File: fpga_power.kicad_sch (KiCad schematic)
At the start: 1 part, among them U2 XC7A50T-2FTG256I

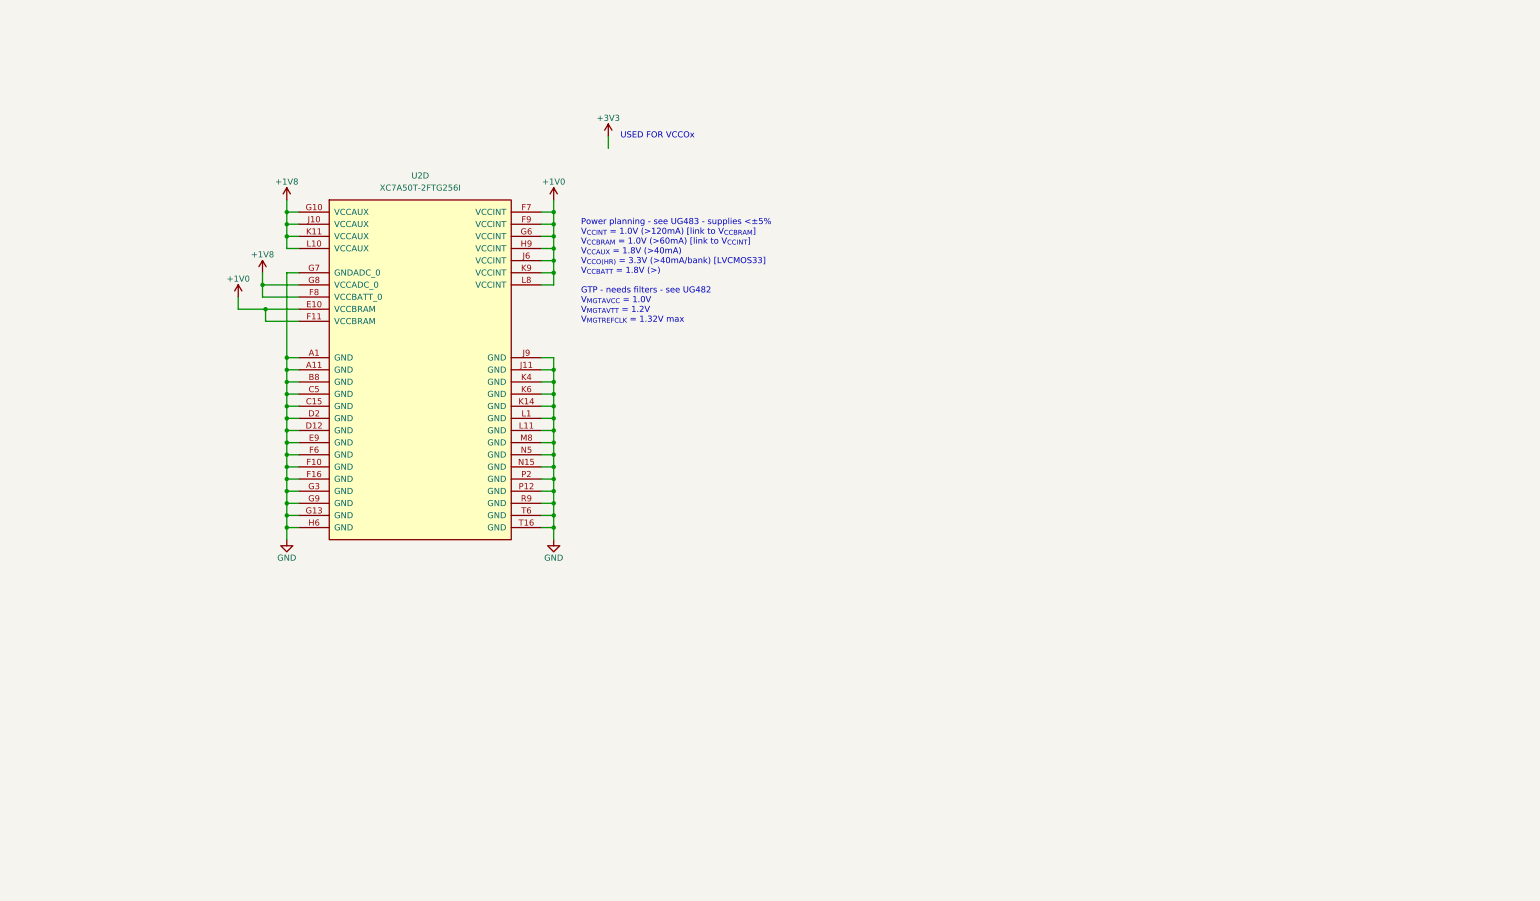
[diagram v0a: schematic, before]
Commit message: Changed FPGA to new package and hooked up some more pins
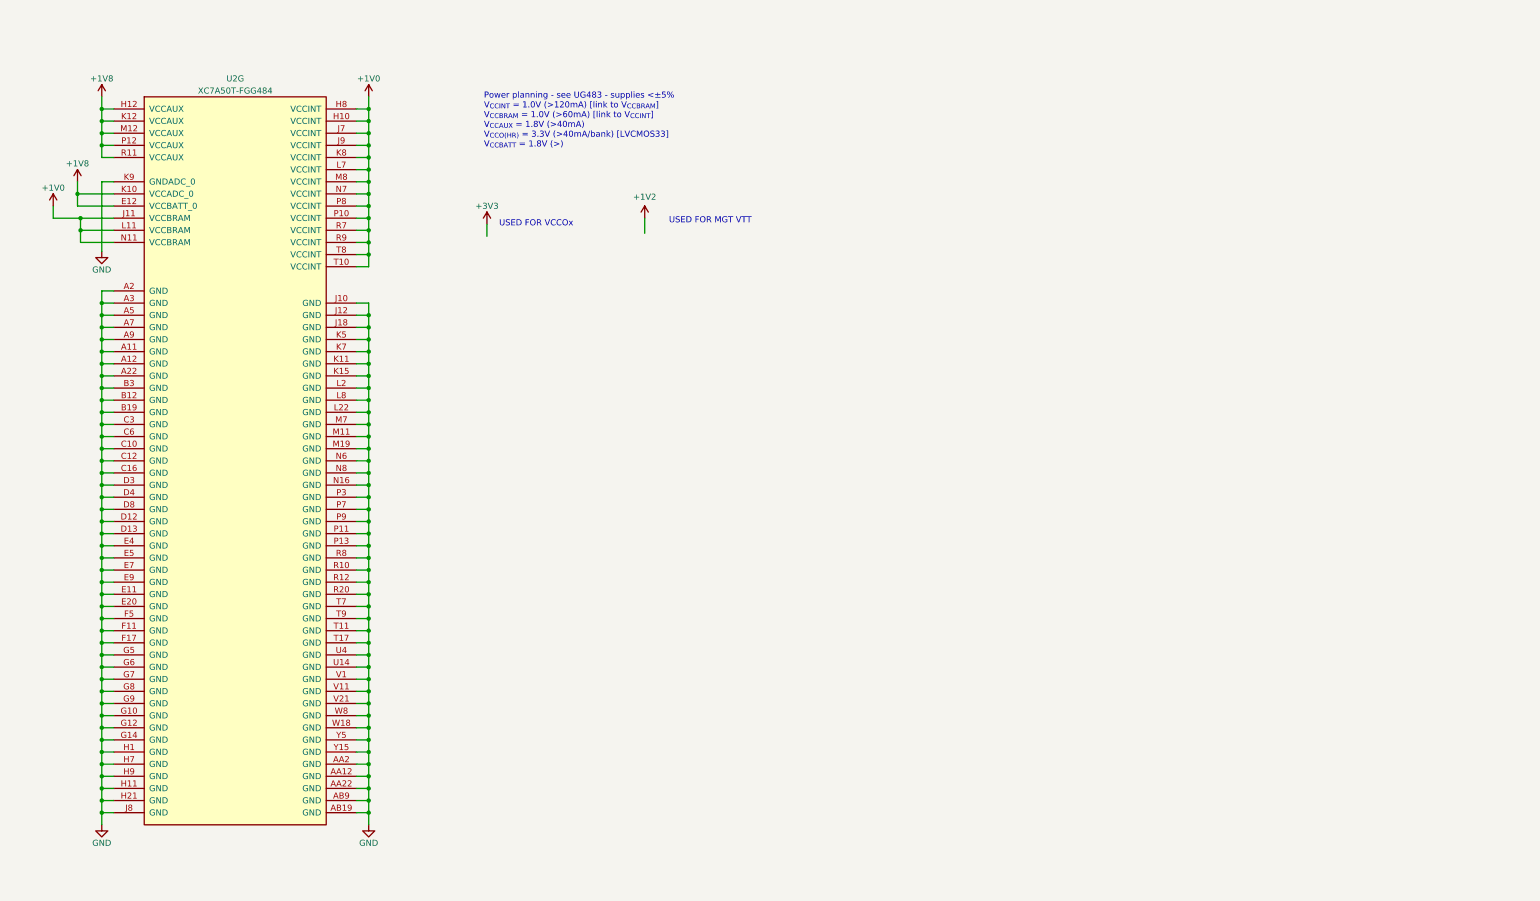
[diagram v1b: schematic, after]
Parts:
- removed U2: XC7A50T-2FTG256I, Package_BGA:Xilinx_FTG256, symbol FPGA_Xilinx_Artix7:XC7A50T-FTG256
- added U2: XC7A50T-FGG484, Package_BGA:Xilinx_FGG484, symbol FPGA_Xilinx_Artix7:XC7A50T-FGG484
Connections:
- net +1V0: now also U2.H10 (VCCINT), U2.H8 (VCCINT), U2.J11 (VCCBRAM), U2.J7 (VCCINT), U2.J9 (VCCINT), U2.K8 (VCCINT), U2.L11 (VCCBRAM), U2.L7 (VCCINT), U2.M8 (VCCINT), U2.N11 (VCCBRAM), U2.N7 (VCCINT), U2.P10 (VCCINT), U2.P8 (VCCINT), U2.R7 (VCCINT), U2.R9 (VCCINT), U2.T10 (VCCINT), U2.T8 (VCCINT)
- net +1V8: now also U2.E12 (VCCBATT_0), U2.H12 (VCCAUX), U2.K10 (VCCADC_0), U2.K12 (VCCAUX), U2.M12 (VCCAUX), U2.P12 (VCCAUX), U2.R11 (VCCAUX)
- net GND: now also U2.A11 (GND), U2.A12 (GND), U2.A2 (GND), U2.A22 (GND), U2.A3 (GND), U2.A5 (GND), U2.A7 (GND), U2.A9 (GND), U2.AA12 (GND), U2.AA2 (GND), U2.AA22 (GND), U2.AB19 (GND), U2.AB9 (GND), U2.B12 (GND), U2.B19 (GND), U2.B3 (GND), U2.C10 (GND), U2.C12 (GND), U2.C16 (GND), U2.C3 (GND), U2.C6 (GND), U2.D12 (GND), U2.D13 (GND), U2.D3 (GND), U2.D4 (GND), U2.D8 (GND), U2.E11 (GND), U2.E20 (GND), U2.E4 (GND), U2.E5 (GND), U2.E7 (GND), U2.E9 (GND), U2.F11 (GND), U2.F17 (GND), U2.F5 (GND), U2.G10 (GND), U2.G12 (GND), U2.G14 (GND), U2.G5 (GND), U2.G6 (GND), U2.G7 (GND), U2.G8 (GND), U2.G9 (GND), U2.H1 (GND), U2.H11 (GND), U2.H21 (GND), U2.H7 (GND), U2.H9 (GND), U2.J10 (GND), U2.J12 (GND), U2.J18 (GND), U2.J8 (GND), U2.K11 (GND), U2.K15 (GND), U2.K5 (GND), U2.K7 (GND), U2.K9 (GNDADC_0), U2.L2 (GND), U2.L22 (GND), U2.L8 (GND), U2.M11 (GND), U2.M19 (GND), U2.M7 (GND), U2.N16 (GND), U2.N6 (GND), U2.N8 (GND), U2.P11 (GND), U2.P13 (GND), U2.P3 (GND), U2.P7 (GND), U2.P9 (GND), U2.R10 (GND), U2.R12 (GND), U2.R20 (GND), U2.R8 (GND), U2.T11 (GND), U2.T17 (GND), U2.T7 (GND), U2.T9 (GND), U2.U14 (GND), U2.U4 (GND), U2.V1 (GND), U2.V11 (GND), U2.V21 (GND), U2.W18 (GND), U2.W8 (GND), U2.Y15 (GND), U2.Y5 (GND)
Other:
- note added: "Power planning - see UG483 - supplies <±5% V_{CCINT} = 1.0V (>120mA) [link to V_{CCBRAM}] V_{CCBRAM} = 1.0V (>60mA) [link to V_{CCINT}] V_{CCAUX} = 1.8V (>40mA) V_{CCO(HR)} = 3.3V (>40mA/bank) [LVCMOS33] V_{CCBATT} = 1.8V (>)"
- note added: "USED FOR MGT VTT"
- note removed: "Power planning - see UG483 - supplies <±5% V_{CCINT} = 1.0V (>120mA) [link to V_{CCBRAM}] V_{CCBRAM} = 1.0V (>60mA) [link to V_{CCINT}] V_{CCAUX} = 1.8V (>40mA) V_{CCO(HR)} = 3.3V (>40mA/bank) [LVCMOS33] V_{CCBATT} = 1.8V (>) GTP - needs filters - see UG482 V_{MGTAVCC} = 1.0V V_{MGTAVTT} = 1.2V V_{MGTREFCLK} = 1.32V max"

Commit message: Schematic finished, starting layout
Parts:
- added C100, C95, C96, C97, C98, C99: 100u, Capacitor_SMD:C_1206_3216Metric_Pad1.33x1.80mm_HandSolder, symbol Device:C_Small
- added C14, C16, C17, C20, C21, C22, C23, C25, C27, C28, C29, C30, C32, C34, C35, C36, C37, C39, C41, C42, C43, C44, C46, C48, C8, C9: 4.7u, Capacitor_SMD:C_0402_1005Metric_Pad0.74x0.62mm_HandSolder, symbol Device:C_Small
- added C18, C24: 4.7n, Capacitor_SMD:C_0402_1005Metric_Pad0.74x0.62mm_HandSolder, symbol Device:C_Small
- added C31: 3.3n, Capacitor_SMD:C_0402_1005Metric_Pad0.74x0.62mm_HandSolder, symbol Device:C_Small
- added C38: 1.5n, Capacitor_SMD:C_0402_1005Metric_Pad0.74x0.62mm_HandSolder, symbol Device:C_Small
- added C45: 2.7n, Capacitor_SMD:C_0402_1005Metric_Pad0.74x0.62mm_HandSolder, symbol Device:C_Small
- added C47: 100n, Capacitor_SMD:C_0402_1005Metric_Pad0.74x0.62mm_HandSolder, symbol Device:C_Small
- added C49, C50, C51, C52, C53: 10n, Capacitor_SMD:C_0402_1005Metric_Pad0.74x0.62mm_HandSolder, symbol Device:C_Small
- added D2: RED, LED_SMD:LED_0603_1608Metric_Pad1.05x0.95mm_HandSolder, symbol Device:LED
- added JP2, JP3, JP4, JP5, JP6: ID_WP, Jumper:SolderJumper-2_P1.3mm_Open_TrianglePad1.0x1.5mm, symbol Jumper:SolderJumper_2_Open
- added R14, R19: 0, Resistor_SMD:R_0402_1005Metric_Pad0.72x0.64mm_HandSolder, symbol Device:R_Small
- added R15, R18: 4.99k, Resistor_SMD:R_0402_1005Metric_Pad0.72x0.64mm_HandSolder, symbol Device:R_Small
- added R16, R17, R20, R21, R23, R26, R30, R31, R32: 1k, Resistor_SMD:R_0402_1005Metric_Pad0.72x0.64mm_HandSolder, symbol Device:R_Small
- added R22: 200, Resistor_SMD:R_0402_1005Metric_Pad0.72x0.64mm_HandSolder, symbol Device:R_Small
- added R24: 1.5k, Resistor_SMD:R_0402_1005Metric_Pad0.72x0.64mm_HandSolder, symbol Device:R_Small
- added R25: 1.2k, Resistor_SMD:R_0402_1005Metric_Pad0.72x0.64mm_HandSolder, symbol Device:R_Small
- added R27: 2.7k, Resistor_SMD:R_0402_1005Metric_Pad0.72x0.64mm_HandSolder, symbol Device:R_Small
- added R28: 6.2k, Resistor_SMD:R_0402_1005Metric_Pad0.72x0.64mm_HandSolder, symbol Device:R_Small
- added R29: 3.9k, Resistor_SMD:R_0402_1005Metric_Pad0.72x0.64mm_HandSolder, symbol Device:R_Small
- added TP1, TP2: TestPoint, TestPoint:TestPoint_Pad_D1.0mm, symbol Connector:TestPoint
- added U3, U4, U5, U6, U7: LP3878MR-ADJ, Package_SO:TI_SO-PowerPAD-8, symbol LP3878SD-ADJ:LP3878SD-ADJ
- added U8: MCP23008-E/ML, Package_DFN_QFN:QFN-20-1EP_4x4mm_P0.5mm_EP2.7x2.7mm, symbol Interface_Expansion:MCP23008-xML
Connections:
- net +1V0: now also JP2.1 (A), JP3.1 (A)
- net +1V2: now also JP4.1 (A)
- net +1V8: now also JP5.1 (A)
- net +3V3: now also JP6.1 (A)
- net GND: now also C100.1, C14.1, C16.1, C17.1, C20.1, C21.1, C22.1, C23.1, C25.1, C27.1, C28.1, C29.1, C30.1, C32.1, C34.1, C35.1, C36.1, C37.1, C39.1, C41.1, C42.1, C43.1, C44.1, C46.1, C47.2, C48.1, C49.2, C50.2, C51.2, C52.2, C53.2, C8.1, C9.1, C95.1, C96.1, C97.1, C98.1, C99.1, D2.1 (K), R15.1, R16.1, R17.1, R18.1, R20.1, R21.1, R23.1, R24.1, R26.1, R27.1, U3.3 (GND), U3.9 (EP), U4.3 (GND), U4.9 (EP), U5.3 (GND), U5.9 (EP), U6.3 (GND), U6.9 (EP), U7.3 (GND), U7.9 (EP), U8.1 (A2), U8.17 (VSS), U8.2 (A1), U8.3 (A0)
- new net: C36.2, C37.2, C38.2, C39.2, C99.2, JP5.2 (B), R25.2, U6.5 (OUT)
- new net: C24.1, R18.2, R19.1, U4.6 (ADJ)
- new net: C22.2, C23.2, C24.2, C25.2, C97.2, JP3.2 (B), R19.2, U4.5 (OUT)
- new net: D2.2 (A), R32.2
- new net: C31.1, R21.2, R22.1, U5.6 (ADJ)
- new net: C51.1, U5.1 (BYP)
- new net: C29.2, C30.2, C31.2, C32.2, C98.2, JP4.2 (B), R22.2, U5.5 (OUT)
- new net: C45.1, R27.2, R28.1, U7.6 (ADJ)
- new net: C18.1, R14.1, R15.2, U3.6 (ADJ)
- new net: C14.2, C16.2, C17.2, C18.2, C95.2, JP2.2 (B), R14.2, U3.5 (OUT)
- new net: C100.2, C43.2, C44.2, C45.2, C46.2, JP6.2 (B), R28.2, U7.5 (OUT)
- new net: C53.1, U7.1 (BYP)
- new net: C48.2, R29.2, U8.4 (~{RESET})
- new net: R32.1, U8.16 (GP7)
- new net: TP1.1, U8.14 (GP5)
- new net: TP2.1, U8.15 (GP6)
- new net: C38.1, R24.2, R25.1, U6.6 (ADJ)
- new net: C49.1, U3.1 (BYP)
- new net: C50.1, U4.1 (BYP)
- new net: C52.1, U6.1 (BYP)
- new net +5V: C20.2, C21.2, C27.2, C28.2, C34.2, C35.2, C41.2, C42.2, C47.1, C8.2, C9.2, C96.2, R29.1, R30.2, R31.2, U3.4 (IN), U4.4 (IN), U5.4 (IN), U6.4 (IN), U7.4 (IN), U8.18 (VDD)
- new net PWR_SCL: R30.1, U8.19 (SCL)
- new net PWR_SDA: R31.1, U8.20 (SDA)
- new net VCCAUX_EN: R23.2, U6.8 (~{SD}), U8.12 (GP3)
- new net VCCINT_EN: R16.2, U3.8 (~{SD}), U8.9 (GP0)
- new net VCCO_EN: R26.2, U7.8 (~{SD}), U8.13 (GP4)
- new net VMGTAVCC_EN: R17.2, U4.8 (~{SD}), U8.10 (GP1)
- new net VMGTAVTT_EN: R20.2, U5.8 (~{SD}), U8.11 (GP2)
- no-connect marks 0 -> 1
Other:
- note added: "1.000V"
- note added: "1.200V"
- note added: "1.800V"
- note added: "3.296V"
- note added: "Address = 0x20"
- note added: "I2C Power Sequencing"
- note added: "Power planning - see UG483 - supplies within ±5% V_{CCINT} = 1.0V (>120mA) [link to V_{CCBRAM}] V_{CCBRAM} = 1.0V (>60mA) [link to V_{CCINT}] V_{CCAUX} = 1.8V (>40mA) V_{CCBATT} = 1.8V [link to V_{CCAUX}] V_{CCO(HR)} = 3.3V (>40mA/bank) [LVCMOS33] V_{MGTAVCC} = 1.0V (>140mA) V_{MGTAVTT} = 1.2V (>140mA) Decouple with 1x4.7uF & 2x0.1uF ceramic 0402/0201 per group. MGT supplies should not share with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"
- note added: "Power sequence controlled by RPi I2C1 through MCP23008."
- note added: "Seq #1 : 1.0V : 200mA : V_{CCINT} + V_{CCBRAM} Seq #2 : 1.0V : 150mA : V_{MGTAVCC} Seq #3 : 1.2V : 150mA : V_{MGTAVTT} Seq #4 : 1.8V : 50mA? : V_{CCAUX} + V_{CCBATT} Seq #5 : 3.3V : 500mA : V_{CCO(HR)}"
- note added: "Seq-#1"
- note added: "Seq-#2"
- note added: "Seq-#3"
- note added: "Seq-#4"
- note added: "Seq-#5"
- note added: "V_{CCAUX} + V_{CCBATT} (1.8V)"
- note added: "V_{CCINT} + V_{CCBRAM} (1.0V)"
- note added: "V_{CCO(HR)} (3.3V)"
- note added: "V_{MGTAVCC} (1.0V)"
- note added: "V_{MGTAVTT} (1.2V)"
- note removed: "Power planning - see UG483 - supplies <±5% V_{CCINT} = 1.0V (>120mA) [link to V_{CCBRAM}] V_{CCBRAM} = 1.0V (>60mA) [link to V_{CCINT}] V_{CCAUX} = 1.8V (>40mA) V_{CCO(HR)} = 3.3V (>40mA/bank) [LVCMOS33] V_{CCBATT} = 1.8V (>)"
- note removed: "USED FOR MGT VTT"
- note removed: "USED FOR VCCOx"
- moved on the sheet: U2G

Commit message: Updated titleblock texts
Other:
- title: FPGA Power -> FPGA Power Supplies & Sequencing
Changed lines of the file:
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@@
   (paper "A4")
   (title_block
-    (title "FPGA Power")
-    (date "2024-02-11")
+    (title "FPGA Power Supplies & Sequencing")
+    (date "2024-02-14")
     (rev "0.1")
     (company "George Smart, M1GEO")
